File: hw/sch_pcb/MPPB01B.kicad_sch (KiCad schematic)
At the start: 15 parts, among them P10 SATA7-67491-1030, P11 HEADER_2x05_PARALLEL, P12 HEADER_2x05_PARALLEL, P5 SAS_mini_1888174-6, P6 SAS_mini_1888174-6, P9 HEADER_2x03_PARALLEL, SW1 Prepinac

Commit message: Edit bom and footprint
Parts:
- C2: value 100uF/10V -> 100uF/6V3
- C3, C4: footprint Capacitor_SMD:C_0805_2012Metric_Pad1.18x1.45mm_HandSolder -> Capacitor_SMD:C_0805_2012Metric
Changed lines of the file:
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@@
       (effects (font (size 1.27 1.27)) (justify left))
     )
-    (property "Value" "100uF/10V" (id 1) (at 80.645 196.215 0)
+    (property "Value" "100uF/6V3" (id 1) (at 80.645 196.215 0)
       (effects (font (size 1.27 1.27)) (justify left))
     )
@@
       (effects (font (size 1.27 1.27)) (justify left))
     )
-    (property "Footprint" "Capacitor_SMD:C_0805_2012Metric_Pad1.18x1.45mm_HandSolder" (id 2) (at 274.32 81.28 0)
+    (property "Footprint" "Capacitor_SMD:C_0805_2012Metric" (id 2) (at 274.32 81.28 0)
       (effects (font (size 1.27 1.27)) hide)
     )
@@
       (effects (font (size 1.27 1.27)) (justify left))
     )
-    (property "Footprint" "Capacitor_SMD:C_0805_2012Metric_Pad1.18x1.45mm_HandSolder" (id 2) (at 273.05 196.85 0)
+    (property "Footprint" "Capacitor_SMD:C_0805_2012Metric" (id 2) (at 273.05 196.85 0)
       (effects (font (size 1.27 1.27)) hide)
     )
@@
     )
     (path "/00000000-0000-0000-0000-00005a3fd70a"
-      (reference "C2") (unit 1) (value "100uF/10V") (footprint "Capacitor_SMD:C_1210_3225Metric")
+      (reference "C2") (unit 1) (value "100uF/6V3") (footprint "Capacitor_SMD:C_1210_3225Metric")
     )
     (path "/00000000-0000-0000-0000-00005a612913"
-      (reference "C3") (unit 1) (value "100nF/16V") (footprint "Capacitor_SMD:C_0805_2012Metric_Pad1.18x1.45mm_HandSolder")
+      (reference "C3") (unit 1) (value "100nF/16V") (footprint "Capacitor_SMD:C_0805_2012Metric")
     )
     (path "/00000000-0000-0000-0000-00005a6379ed"
-      (reference "C4") (unit 1) (value "100nF/16V") (footprint "Capacitor_SMD:C_0805_2012Metric_Pad1.18x1.45mm_HandSolder")
+      (reference "C4") (unit 1) (value "100nF/16V") (footprint "Capacitor_SMD:C_0805_2012Metric")
     )
     (path "/00000000-0000-0000-0000-00005a3fd25b"

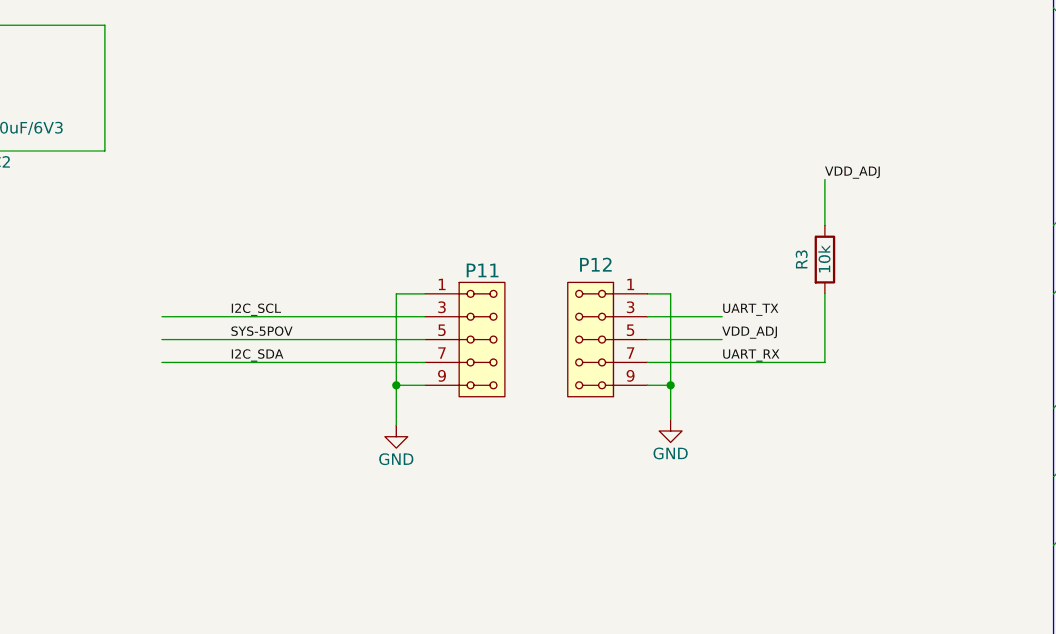
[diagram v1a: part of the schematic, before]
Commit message: Improve connector pinout #2
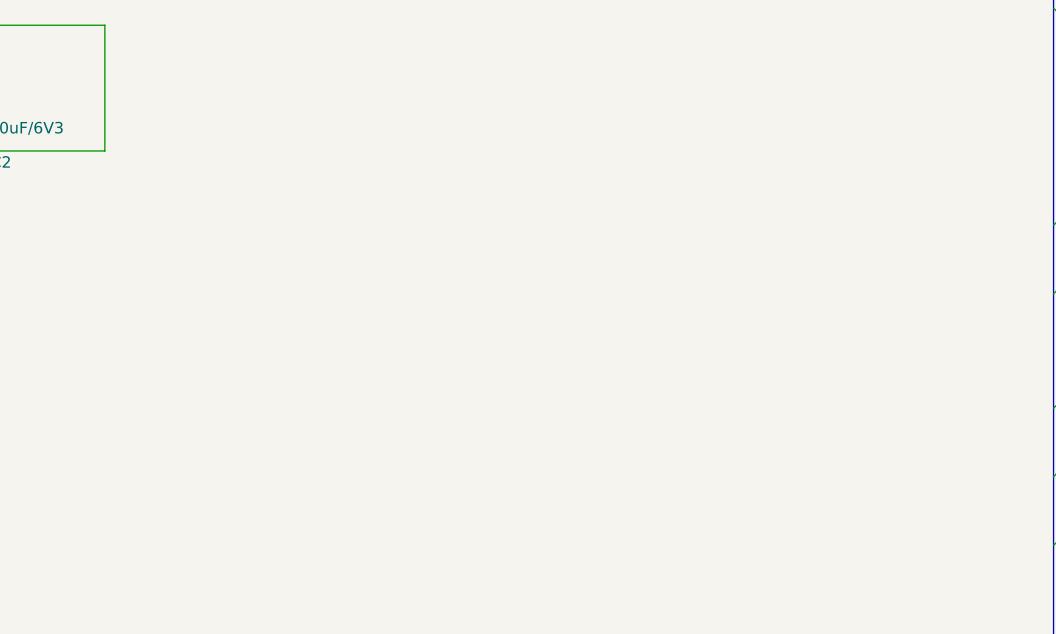
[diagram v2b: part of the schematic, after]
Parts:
- removed P11, P12: HEADER_2x05_PARALLEL, Mlab_Pin_Headers:Straight_2x05, symbol MLAB_HEADER:HEADER_2x05_PARALLEL
- removed R3: 10k, Resistor_SMD:R_0805_2012Metric_Pad1.20x1.40mm_HandSolder, symbol paracard-template-rescue:R-device

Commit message: pridani UST_ID
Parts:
- C1, C3, C4: UST_ID (none) -> 5c70984712875079b91f8b4c
- C2: UST_ID (none) -> 5c70984712875079b91f8b80
- D1: UST_ID (none) -> 5c70984512875079b91f88ac
- P10: UST_ID (none) -> 5c70984712875079b91f8a7b
- P5, P6: UST_ID (none) -> 624ede60592c2d62176d5a96
- R1, R2: UST_ID (none) -> 5c70984512875079b91f8977
- SW1: UST_ID (none) -> 5c70984712875079b91f8ad1
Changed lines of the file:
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@@
       (effects (font (size 1.524 1.524)))
+    )
+    (property "UST_ID" "624ede60592c2d62176d5a96" (id 4) (at 262.89 67.31 0)
+      (effects (font (size 1.27 1.27)) hide)
     )
     (pin "1")
@@
     (property "Datasheet" "" (id 3) (at 273.05 90.17 0)
       (effects (font (size 1.524 1.524)))
+    )
+    (property "UST_ID" "624ede60592c2d62176d5a96" (id 4) (at 262.89 91.44 0)
+      (effects (font (size 1.27 1.27)) hide)
     )
     (pin "5")
@@
       (effects (font (size 1.524 1.524)))
     )
+    (property "UST_ID" "624ede60592c2d62176d5a96" (id 4) (at 262.89 182.88 0)
+      (effects (font (size 1.27 1.27)) hide)
+    )
     (pin "1")
     (pin "2")
@@
     (property "Datasheet" "" (id 3) (at 273.05 205.74 0)
       (effects (font (size 1.524 1.524)))
+    )
+    (property "UST_ID" "624ede60592c2d62176d5a96" (id 4) (at 262.89 207.01 0)
+      (effects (font (size 1.27 1.27)) hide)
     )
     (pin "5")
@@
       (effects (font (size 1.524 1.524)))
     )
+    (property "UST_ID" "5c70984712875079b91f8a7b" (id 4) (at 140.97 38.1 0)
+      (effects (font (size 1.27 1.27)) hide)
+    )
     (pin "1")
     (pin "2")
@@
       (effects (font (size 1.27 1.27)) hide)
     )
+    (property "UST_ID" "5c70984512875079b91f88ac" (id 4) (at 67.945 202.565 0)
+      (effects (font (size 1.27 1.27)) hide)
+    )
     (pin "1")
     (pin "2")
@@
       (effects (font (size 1.27 1.27)) hide)
     )
+    (property "UST_ID" "5c70984712875079b91f8b4c" (id 4) (at 74.295 202.565 0)
+      (effects (font (size 1.27 1.27)) hide)
+    )
     (pin "1")
     (pin "2")
@@
     )
     (property "Datasheet" "" (id 3) (at 80.645 202.565 0)
+      (effects (font (size 1.27 1.27)) hide)
+    )
+    (property "UST_ID" "5c70984712875079b91f8b80" (id 4) (at 80.645 202.565 0)
       (effects (font (size 1.27 1.27)) hide)
     )
@@
       (effects (font (size 1.27 1.27)) hide)
     )
+    (property "UST_ID" "5c70984512875079b91f8977" (id 4) (at 274.32 76.2 0)
+      (effects (font (size 1.27 1.27)) hide)
+    )
     (pin "1")
     (pin "2")
@@
       (effects (font (size 1.27 1.27)) hide)
     )
+    (property "UST_ID" "5c70984512875079b91f8977" (id 4) (at 273.05 191.77 0)
+      (effects (font (size 1.27 1.27)) hide)
+    )
     (pin "1")
     (pin "2")
@@
     )
     (property "Datasheet" "" (id 3) (at 274.32 81.28 0)
+      (effects (font (size 1.27 1.27)) hide)
+    )
+    (property "UST_ID" "5c70984712875079b91f8b4c" (id 4) (at 274.32 81.28 0)
       (effects (font (size 1.27 1.27)) hide)
     )
@@
       (effects (font (size 1.27 1.27)) hide)
     )
+    (property "UST_ID" "5c70984712875079b91f8b4c" (id 4) (at 273.05 196.85 0)
+      (effects (font (size 1.27 1.27)) hide)
+    )
     (pin "1")
     (pin "2")
@@
     )
     (property "Datasheet" "" (id 3) (at 193.675 146.685 0))
-    (pin "1")
-    (pin "2")
+    (property "UST_ID" "5c70984712875079b91f8ad1" (id 4) (at 193.675 146.685 0)
+      (effects (font (size 1.27 1.27)) hide)
+    )
+    (pin "1")
+    (pin "2")

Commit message: Priprava pro osazeni
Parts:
- C1, C3, C4: value 100nF/16V -> (none); footprint Capacitor_SMD:C_0805_2012Metric -> (none)
- C2: value 100uF/6V3 -> (none); footprint Capacitor_SMD:C_1210_3225Metric -> (none)
- D1: value M4 -> (none); footprint Diode_SMD:D_SMA -> (none)
- P10: value SATA7-67491-1030 -> (none); footprint Mlab_CON:SATA-7_THT_VERT_2 -> (none)
- P5, P6: value SAS_mini_1888174-6 -> (none); footprint Mlab_CON:SAS-mini_TEConnectivity_1888174_Vertical -> (none)
- P9: value HEADER_2x03_PARALLEL -> (none); footprint Mlab_Pin_Headers:Straight_2x03 -> (none)
- R1, R2: value 100 -> (none); footprint Resistor_SMD:R_0805_2012Metric_Pad1.20x1.40mm_HandSolder -> (none)
- SW1: value Prepinac -> (none); footprint Mlab_SW:SW_PUSH_SMALL -> (none)
